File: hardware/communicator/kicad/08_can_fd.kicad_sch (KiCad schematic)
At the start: 10 parts, among them U20 TCAN1046AVDYYRQ1, U21 SN74LVC2G17DCKR

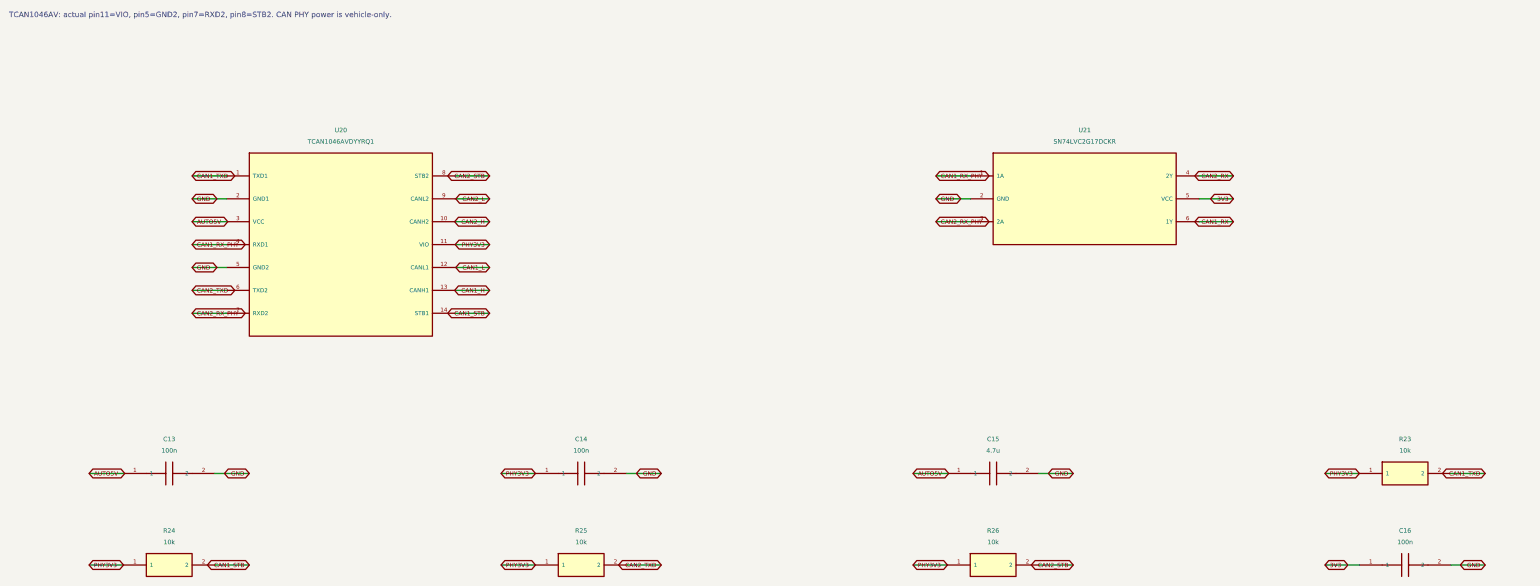
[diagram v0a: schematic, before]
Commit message: feat: add R1 detailed hardware and navigation protocol review candidate
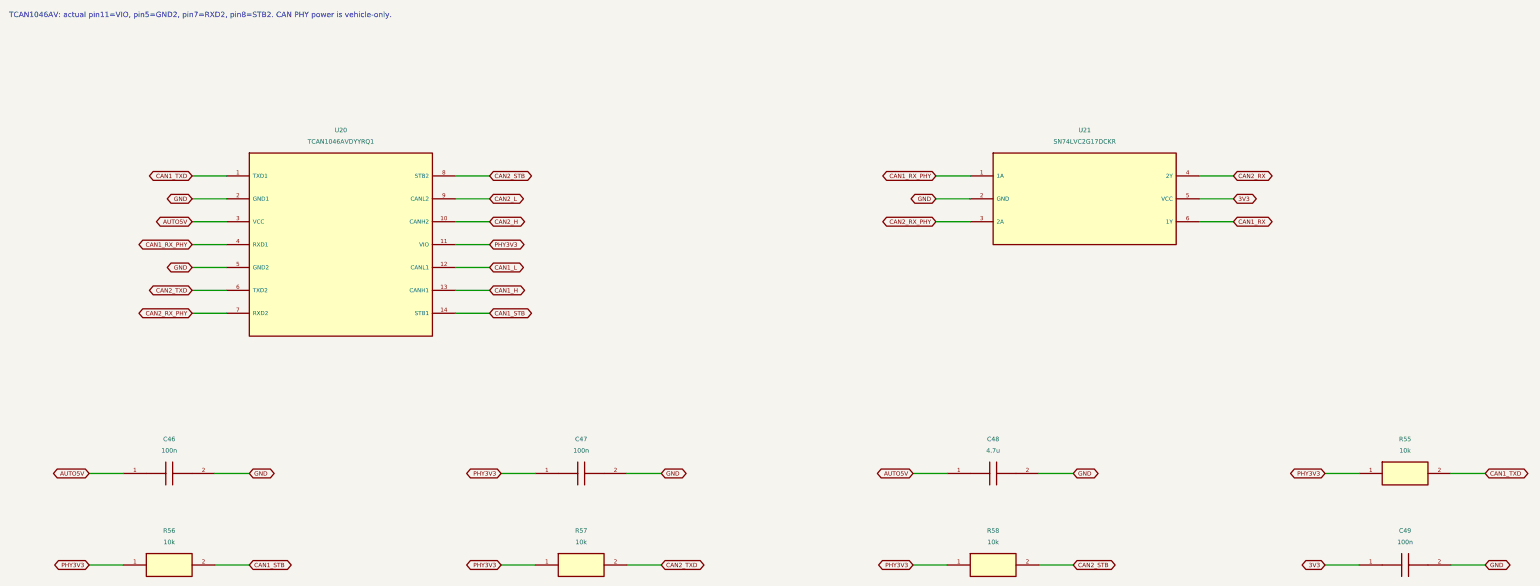
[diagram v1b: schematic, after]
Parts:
- removed C13: 100n, CANView:Capacitor_SMD__C_0402_1005Metric, symbol CANView:CANView_communicator_C13
- removed C14: 100n, CANView:Capacitor_SMD__C_0402_1005Metric, symbol CANView:CANView_communicator_C14
- removed C15: 4.7u, CANView:Capacitor_SMD__C_0603_1608Metric, symbol CANView:CANView_communicator_C15
- removed C16: 100n, CANView:Capacitor_SMD__C_0402_1005Metric, symbol CANView:CANView_communicator_C16
- removed R23: 10k, CANView:Resistor_SMD__R_0402_1005Metric, symbol CANView:CANView_communicator_R23
- removed R24: 10k, CANView:Resistor_SMD__R_0402_1005Metric, symbol CANView:CANView_communicator_R24
- removed R25: 10k, CANView:Resistor_SMD__R_0402_1005Metric, symbol CANView:CANView_communicator_R25
- removed R26: 10k, CANView:Resistor_SMD__R_0402_1005Metric, symbol CANView:CANView_communicator_R26
- added C46: 100n, CANView:Capacitor_SMD__C_0402_1005Metric, symbol CANView:CANView_communicator_C46
- added C47: 100n, CANView:Capacitor_SMD__C_0402_1005Metric, symbol CANView:CANView_communicator_C47
- added C48: 4.7u, CANView:Capacitor_SMD__C_0603_1608Metric, symbol CANView:CANView_communicator_C48
- added C49: 100n, CANView:Capacitor_SMD__C_0402_1005Metric, symbol CANView:CANView_communicator_C49
- added R55: 10k, CANView:Resistor_SMD__R_0402_1005Metric, symbol CANView:CANView_communicator_R55
- added R56: 10k, CANView:Resistor_SMD__R_0402_1005Metric, symbol CANView:CANView_communicator_R56
- added R57: 10k, CANView:Resistor_SMD__R_0402_1005Metric, symbol CANView:CANView_communicator_R57
- added R58: 10k, CANView:Resistor_SMD__R_0402_1005Metric, symbol CANView:CANView_communicator_R58
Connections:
- net 3V3: now also C49.1
- net AUTO5V: now also C46.1, C48.1
- net CAN1_STB: now also R56.2
- net CAN1_TXD: now also R55.2
- net CAN2_STB: now also R58.2
- net CAN2_TXD: now also R57.2
- net GND: now also C46.2, C47.2, C48.2, C49.2
- net PHY3V3: now also C47.1, R55.1, R56.1, R57.1, R58.1

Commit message: fix: close hardware rail-fault paths and sensor contract gaps
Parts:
- removed C46: 100n, CANView:Capacitor_SMD__C_0402_1005Metric, symbol CANView:CANView_communicator_C46
- removed C47: 100n, CANView:Capacitor_SMD__C_0402_1005Metric, symbol CANView:CANView_communicator_C47
- removed R55: 10k, CANView:Resistor_SMD__R_0402_1005Metric, symbol CANView:CANView_communicator_R55
- added C50: 4.7u, CANView:Capacitor_SMD__C_0603_1608Metric, symbol CANView:CANView_communicator_C50
- added C51: 100n, CANView:Capacitor_SMD__C_0402_1005Metric, symbol CANView:CANView_communicator_C51
- added R59: 10k, CANView:Resistor_SMD__R_0402_1005Metric, symbol CANView:CANView_communicator_R59
- C48: value 4.7u -> 100n; footprint CANView:Capacitor_SMD__C_0603_1608Metric -> CANView:Capacitor_SMD__C_0402_1005Metric; MPN GEN-C-0603-4.7u-16V-X7R -> GEN-C-0402-100n-16V-X7R
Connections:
- net 3V3: now also C51.1; no longer C49.1
- net AUTO5V: now also C50.1
- net CAN1_STB: now also R57.2; no longer R56.2
- net CAN1_TXD: now also R56.2
- net CAN2_STB: now also R59.2; no longer R58.2
- net CAN2_TXD: now also R58.2; no longer R57.2
- net GND: now also C50.2, C51.2
- net PHY3V3: now also C49.1, R59.1
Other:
- moved on the sheet: C48, C49, R56, R57, R58
